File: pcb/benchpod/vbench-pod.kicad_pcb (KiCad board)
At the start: 4 copper layers, 100 x 80 mm, 505 parts, among them J1 Conn_02x10_Odd_Even, J4 Screw_Terminal_01x02, J5 Screw_Terminal_01x02, J6 Screw_Terminal_01x02, J7 HR911105A_C12074, J8 Screw_Terminal_01x02, J9 Screw_Terminal_01x02, K1 G6K-2F-Y DC5, K2 G6K-2F-Y DC5, K3 G6K-2F-Y DC5, K4 G6K-2F-Y DC5, Q1 BCP56, SW1 TS-1088-AR02016, SW2 TS-1088-AR02016, U1 ICE40UP5K-SG48ITR, U10 TCAN1044VDRBRQ1, U18 SN74LVC2G66DCUR, U19 SN74LVC2G66DCUR, U2 W25Q64JVSSIQ, U20 SN74LVC2G66DCUR, U21 SN74LVC2G66DCUR, U22 SRV05-4.TCT, U23 SRV05-4.TCT, U24 SN74LVC2G66DCUR, U25 SRV05-4.TCT, U26 TPS259470ARPWR, U27 TPS259470ARPWR, U29 INA238AIDGSR, U3 TPS7A2050PDBVR, U30 TPS82130SILR, U31 AP2112K-1.2, U32 AP2112K-2.5TRG1, U33 INA238AIDGSR, U34 SRV05-4.TCT, U36 MCP33131D-10-E/MS, U37 THS4551IDGKR, U38 ADR4540BRZ-R7, U39 AP2112K-1.8TRG1, U4 ESP32-C3-MINI-1-N4, U40 OPA810IDBVR, U41 LM27761DSGR, U42 LM7705MM/NOPB, U43 DAC8551IADGKR, U44 OPA2365AIDR, U45 OPA2992IDR, U46 AP2112K-3.3, U47 TMUX1104DGSR, U48 TMUX1104DGSR, U49 TPS65131TRGERQ1, U5 STM32H563ZIT6, U50 TPS7A1901DRBR, U51 OPA2992IDR, U52 AP2112K-1.8TRG1, U53 TPL7407LAPWR, U54 TCA9554PWR, U55 TCA9554PWR, U56 TCA9554PWR, U57 TPS259470ARPWR, U58 TCA9554PWR, U6 LAN8742AI-CZ-TR, U7 APS6404L-3SQR-SN_C5333729, U8 TPS2116DRLR, U9 XTR116UA/2K5, X1 SX3M48.000B10F20TNN, Y1 Crystal_GND24, Y2 Crystal_GND24

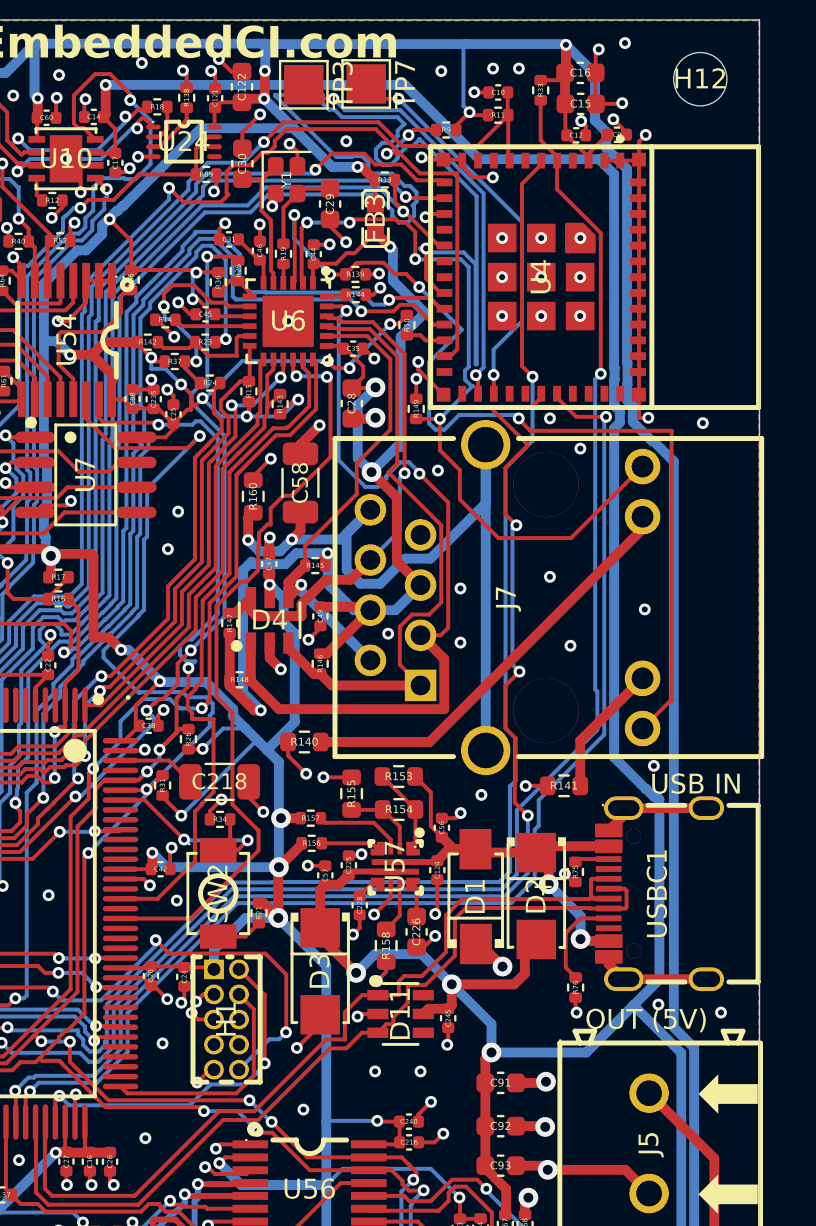
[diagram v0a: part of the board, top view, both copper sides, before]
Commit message: switched D1, added rules area with keepout
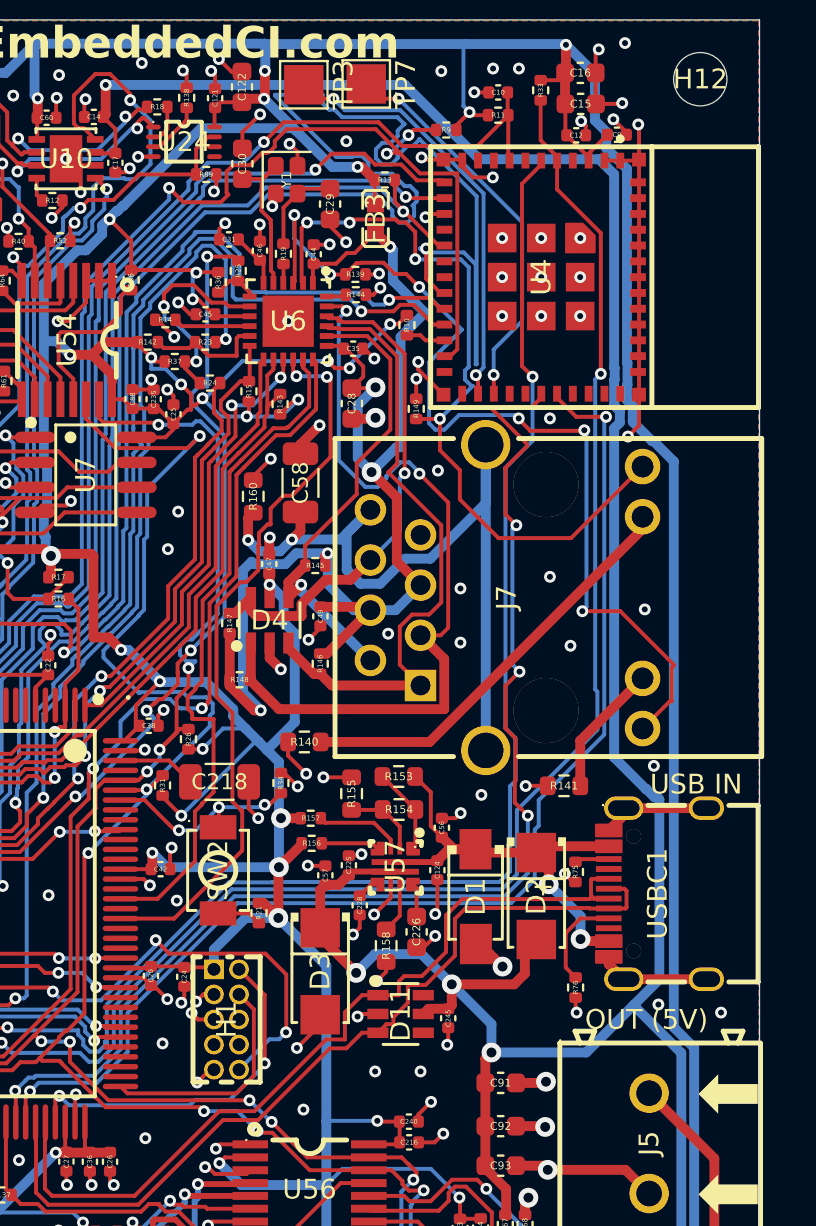
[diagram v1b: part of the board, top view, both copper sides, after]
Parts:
- D15, D16, D2, D3: value SS34_C8678 -> SS34
- moved R34 3.59 mm to (114.8, 58.8), turned to -90 degrees
- moved SW2 1.17 mm to (111.6, 63.2)
- turned D1 to -90 degrees
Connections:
- D1 pad 1: GND -> +5V_EFUSE
- D1 pad 2: +5V_EFUSE -> GND
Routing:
- net GND: track 514.0 -> 516.0 mm, vias 498 -> 496
- net /RMII_TX_EN: track 38.7 -> 37.6 mm
- net /Ethernet/GREEN_LED: track 49.8 -> 48.7 mm, vias 4 -> 6
- net /STM32_BOOT0: track 10.8 -> 10.6 mm, vias 2 -> 3
